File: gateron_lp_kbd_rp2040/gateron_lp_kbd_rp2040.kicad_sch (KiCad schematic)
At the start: 238 parts, among them J1 TYPE-C-31-M-12, J2 JST-SH-2 SM02B, Q1 DMG3415U, SW1 KS-33, SW10 KS-33, SW11 KS-33, SW12 KS-33, SW13 KS-33, SW14 KS-33, SW15 KS-33, SW16 KS-33, SW17 KS-33, SW18 KS-33, SW19 KS-33, SW2 KS-33, SW20 KS-33, SW21 KS-33, SW22 KS-33, SW23 KS-33, SW24 KS-33, SW25 KS-33, SW26 KS-33, SW27 KS-33, SW28 KS-33, SW29 KS-33, SW3 KS-33, SW30 KS-33, SW31 KS-33, SW32 KS-33, SW33 KS-33, SW34 KS-33, SW35 KS-33, SW36 KS-33, SW37 KS-33, SW38 KS-33, SW39 KS-33, SW4 KS-33, SW40 KS-33, SW41 KS-33, SW42 KS-33, SW43 KS-33, SW44 KS-33, SW45 KS-33, SW46 KS-33, SW47 KS-33, SW48 KS-33, SW49 KS-33, SW5 KS-33, SW50 KS-33, SW51 KS-33, SW52 KS-33, SW53 KS-33, SW54 2U, SW55 KS-33, SW56 KS-33, SW57 KS-33, SW58 KS-33, SW59 KS-33, SW6 KS-33, SW60 RESET, SW61 BOOTSEL (VERIFY), SW62 PWR MSK-12C02, SW7 KS-33, SW8 KS-33, SW9 KS-33, U1 RP2040, U2 MCP73831-2ACI/OT, U3 AP2112K-3.3, U4 USBLC6-2SC6, U5 W25Q16JVUXIQ, U6 CYW43439, U7 74AHCT1G125, Y1 12MHz, Y2 37.4MHz

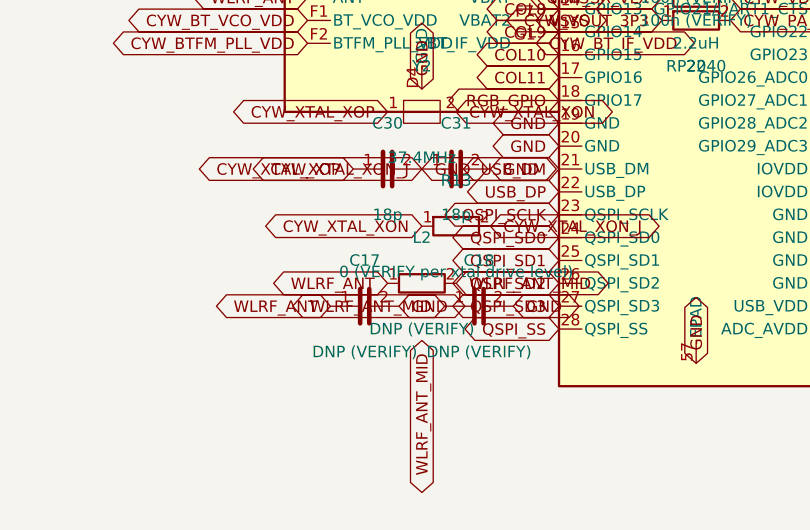
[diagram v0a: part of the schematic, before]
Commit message: Ground CYW43439 antenna matching in Raspberry Pi's real Pico W design
Cross-checked L2/C17/C18 and the crystal load caps against Raspberry Pi's
public Pico W hardware design files (same CYW43439 die, confirms 37.4MHz).
Real component families found there: 4.7nH match inductor, 27pF crystal
load caps, and a documented 0.2-2pF antenna tuning-cap family -- Pico W's
own BOM shows even Raspberry Pi tunes this network per-board rather than
using one fixed value, so C18 is left DNP pending real tuning here too.

Co-Authored-By: Claude Sonnet 5 <noreply@anthropic.com>
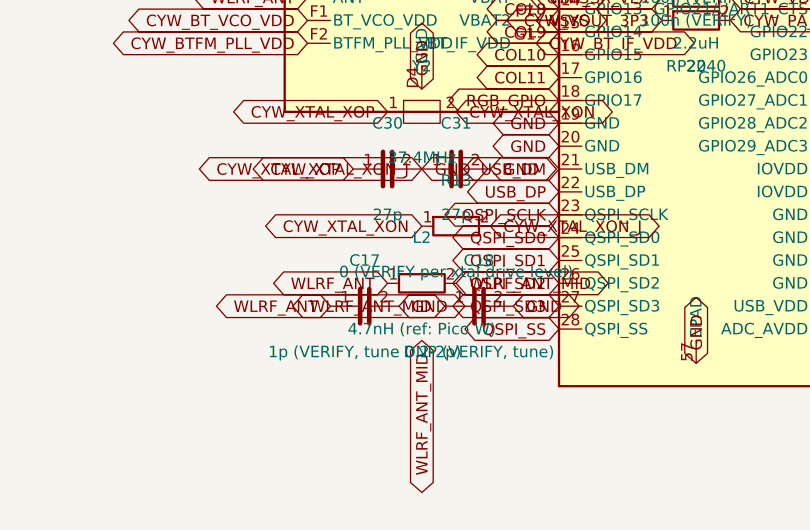
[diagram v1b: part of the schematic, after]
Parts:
- C17: value DNP (VERIFY) -> 1p (VERIFY, tune 0.2-2p)
- C18: value DNP (VERIFY) -> DNP (VERIFY, tune)
- C30, C31: value 18p -> 27p
- L2: value DNP (VERIFY) -> 4.7nH (ref: Pico W)
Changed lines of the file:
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@@
     (exclude_from_sim no) (in_bom yes) (on_board yes) (dnp no) (fields_autoplaced yes)
     (property "Reference" "C30" (at 92.71 176.53 0) (effects (font (size 1.27 1.27))))
-    (property "Value" "18p" (at 92.71 186.69 0) (effects (font (size 1.27 1.27))))
+    (property "Value" "27p" (at 92.71 186.69 0) (effects (font (size 1.27 1.27))))
     (property "Footprint" "kbd:RC_0603" (at 92.71 181.61 0) (effects (font (size 1.27 1.27)) (hide yes)))
     (property "Datasheet" "~" (at 92.71 181.61 0) (effects (font (size 1.27 1.27)) (hide yes)))
@@
     (exclude_from_sim no) (in_bom yes) (on_board yes) (dnp no) (fields_autoplaced yes)
     (property "Reference" "C31" (at 100.33 176.53 0) (effects (font (size 1.27 1.27))))
-    (property "Value" "18p" (at 100.33 186.69 0) (effects (font (size 1.27 1.27))))
+    (property "Value" "27p" (at 100.33 186.69 0) (effects (font (size 1.27 1.27))))
     (property "Footprint" "kbd:RC_0603" (at 100.33 181.61 0) (effects (font (size 1.27 1.27)) (hide yes)))
     (property "Datasheet" "~" (at 100.33 181.61 0) (effects (font (size 1.27 1.27)) (hide yes)))
@@
     (exclude_from_sim no) (in_bom yes) (on_board yes) (dnp no) (fields_autoplaced yes)
     (property "Reference" "L2" (at 96.52 189.23 0) (effects (font (size 1.27 1.27))))
-    (property "Value" "DNP (VERIFY)" (at 96.52 199.39 0) (effects (font (size 1.27 1.27))))
+    (property "Value" "4.7nH (ref: Pico W)" (at 96.52 199.39 0) (effects (font (size 1.27 1.27))))
     (property "Footprint" "kbd:RC_0603" (at 96.52 194.31 0) (effects (font (size 1.27 1.27)) (hide yes)))
     (property "Datasheet" "~" (at 96.52 194.31 0) (effects (font (size 1.27 1.27)) (hide yes)))
@@
     (exclude_from_sim no) (in_bom yes) (on_board yes) (dnp no) (fields_autoplaced yes)
     (property "Reference" "C17" (at 90.17 191.77 0) (effects (font (size 1.27 1.27))))
-    (property "Value" "DNP (VERIFY)" (at 90.17 201.93 0) (effects (font (size 1.27 1.27))))
+    (property "Value" "1p (VERIFY, tune 0.2-2p)" (at 90.17 201.93 0) (effects (font (size 1.27 1.27))))
     (property "Footprint" "kbd:RC_0603" (at 90.17 196.85 0) (effects (font (size 1.27 1.27)) (hide yes)))
     (property "Datasheet" "~" (at 90.17 196.85 0) (effects (font (size 1.27 1.27)) (hide yes)))
@@
     (exclude_from_sim no) (in_bom yes) (on_board yes) (dnp no) (fields_autoplaced yes)
     (property "Reference" "C18" (at 102.87 191.77 0) (effects (font (size 1.27 1.27))))
-    (property "Value" "DNP (VERIFY)" (at 102.87 201.93 0) (effects (font (size 1.27 1.27))))
+    (property "Value" "DNP (VERIFY, tune)" (at 102.87 201.93 0) (effects (font (size 1.27 1.27))))
     (property "Footprint" "kbd:RC_0603" (at 102.87 196.85 0) (effects (font (size 1.27 1.27)) (hide yes)))
     (property "Datasheet" "~" (at 102.87 196.85 0) (effects (font (size 1.27 1.27)) (hide yes)))

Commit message: Match antenna-network footprints to real component package sizes
L2/C17/C18 were using the generic 0603-imperial footprint shared by this
file's other passives, but the real Pico W reference parts are smaller:
the antenna-match inductor is 0201 imperial (Murata LQP03TN4N7H02D, the
DigiKey-listed substitute for the now-obsolete Cyntec original) and the
Murata GJM1555C1H tuning-cap family is 0402 imperial. Added fp_0201/
fp_0402 land patterns and switched L2 to 0201, C17/C18 to 0402.

Co-Authored-By: Claude Sonnet 5 <noreply@anthropic.com>
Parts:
- C17, C18: footprint kbd:RC_0603 -> kbd:RC_0402
- L2: footprint kbd:RC_0603 -> kbd:RC_0201
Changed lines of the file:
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@@
     (property "Reference" "L2" (at 96.52 189.23 0) (effects (font (size 1.27 1.27))))
     (property "Value" "4.7nH (ref: Pico W)" (at 96.52 199.39 0) (effects (font (size 1.27 1.27))))
-    (property "Footprint" "kbd:RC_0603" (at 96.52 194.31 0) (effects (font (size 1.27 1.27)) (hide yes)))
+    (property "Footprint" "kbd:RC_0201" (at 96.52 194.31 0) (effects (font (size 1.27 1.27)) (hide yes)))
     (property "Datasheet" "~" (at 96.52 194.31 0) (effects (font (size 1.27 1.27)) (hide yes)))
     (property "Description" "" (at 96.52 194.31 0) (effects (font (size 1.27 1.27)) (hide yes)))
@@
     (property "Reference" "C17" (at 90.17 191.77 0) (effects (font (size 1.27 1.27))))
     (property "Value" "1p (VERIFY, tune 0.2-2p)" (at 90.17 201.93 0) (effects (font (size 1.27 1.27))))
-    (property "Footprint" "kbd:RC_0603" (at 90.17 196.85 0) (effects (font (size 1.27 1.27)) (hide yes)))
+    (property "Footprint" "kbd:RC_0402" (at 90.17 196.85 0) (effects (font (size 1.27 1.27)) (hide yes)))
     (property "Datasheet" "~" (at 90.17 196.85 0) (effects (font (size 1.27 1.27)) (hide yes)))
     (property "Description" "" (at 90.17 196.85 0) (effects (font (size 1.27 1.27)) (hide yes)))
@@
     (property "Reference" "C18" (at 102.87 191.77 0) (effects (font (size 1.27 1.27))))
     (property "Value" "DNP (VERIFY, tune)" (at 102.87 201.93 0) (effects (font (size 1.27 1.27))))
-    (property "Footprint" "kbd:RC_0603" (at 102.87 196.85 0) (effects (font (size 1.27 1.27)) (hide yes)))
+    (property "Footprint" "kbd:RC_0402" (at 102.87 196.85 0) (effects (font (size 1.27 1.27)) (hide yes)))
     (property "Datasheet" "~" (at 102.87 196.85 0) (effects (font (size 1.27 1.27)) (hide yes)))
     (property "Description" "" (at 102.87 196.85 0) (effects (font (size 1.27 1.27)) (hide yes)))

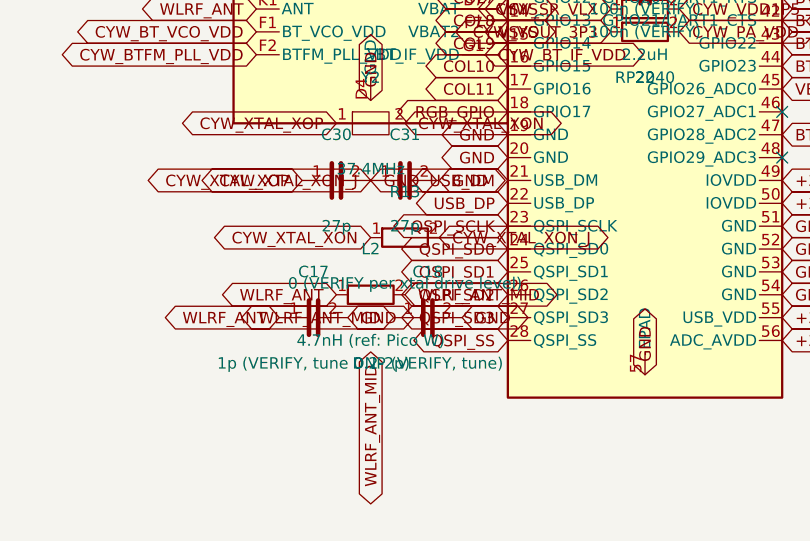
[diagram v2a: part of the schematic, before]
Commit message: Confirm crystal load caps and series resistor against Pico W reference
C30/C31 (27pF) and R13 (0R) were already set to these values but flagged
VERIFY -- re-checked against Raspberry Pi's public Pico W design files
with reference-designator-level evidence this time (not just proximity in
the raw dump): C257/C258 map 1:1 to the 27pF footprint, exactly the pair
a crystal load network needs, and a 0R chip resistor sits on the wireless
chip's crystal clock net. 27pF externals also check out physically
(~15.5-18.5pF effective load cap with typical stray, a standard CL rating).
No value changes, just upgraded confidence and updated comments.

Co-Authored-By: Claude Sonnet 5 <noreply@anthropic.com>
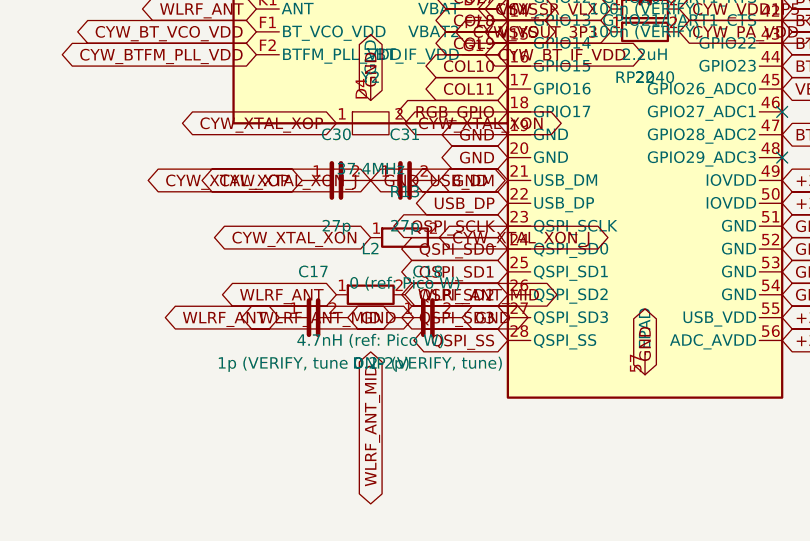
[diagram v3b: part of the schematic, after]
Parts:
- R13: value 0 (VERIFY per xtal drive level) -> 0 (ref: Pico W)
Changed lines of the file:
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@@
     (exclude_from_sim no) (in_bom yes) (on_board yes) (dnp no) (fields_autoplaced yes)
     (property "Reference" "R13" (at 100.33 182.88 0) (effects (font (size 1.27 1.27))))
-    (property "Value" "0 (VERIFY per xtal drive level)" (at 100.33 193.04 0) (effects (font (size 1.27 1.27))))
+    (property "Value" "0 (ref: Pico W)" (at 100.33 193.04 0) (effects (font (size 1.27 1.27))))
     (property "Footprint" "kbd:RC_0603" (at 100.33 187.96 0) (effects (font (size 1.27 1.27)) (hide yes)))
     (property "Datasheet" "~" (at 100.33 187.96 0) (effects (font (size 1.27 1.27)) (hide yes)))
